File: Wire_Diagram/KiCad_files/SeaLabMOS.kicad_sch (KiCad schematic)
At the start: 17 parts

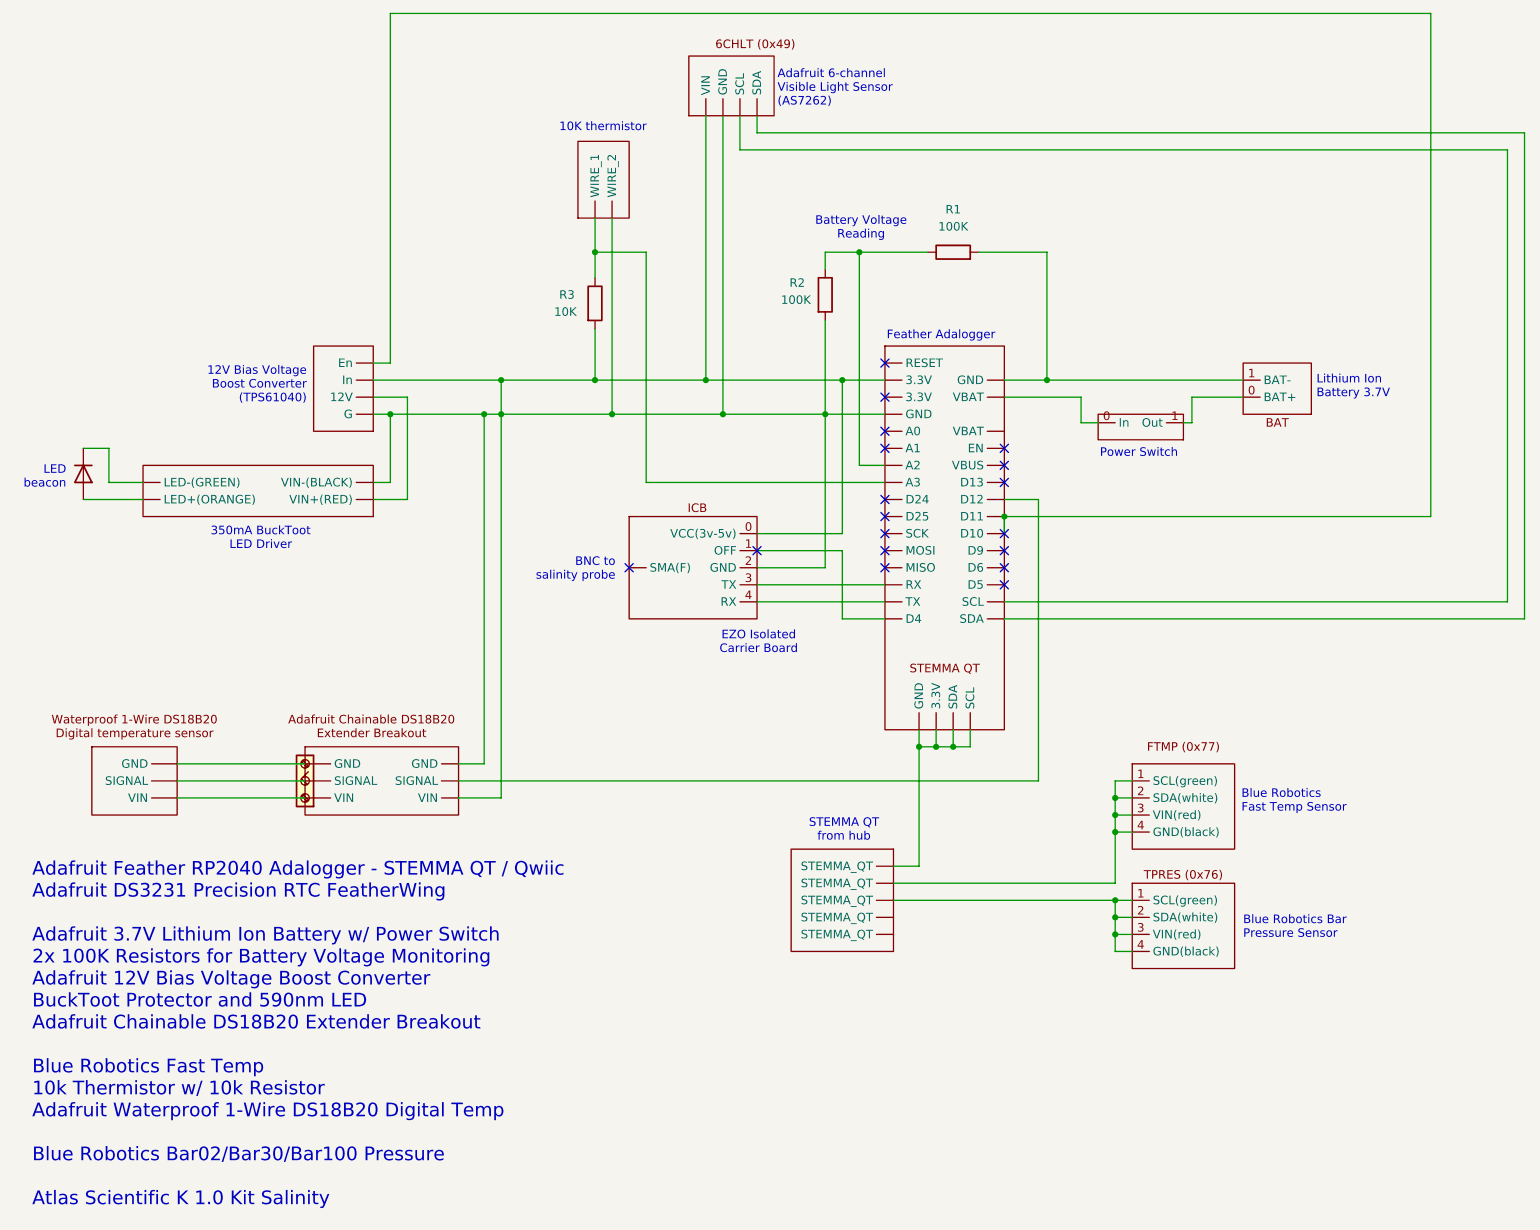
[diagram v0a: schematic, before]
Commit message: added GNSS
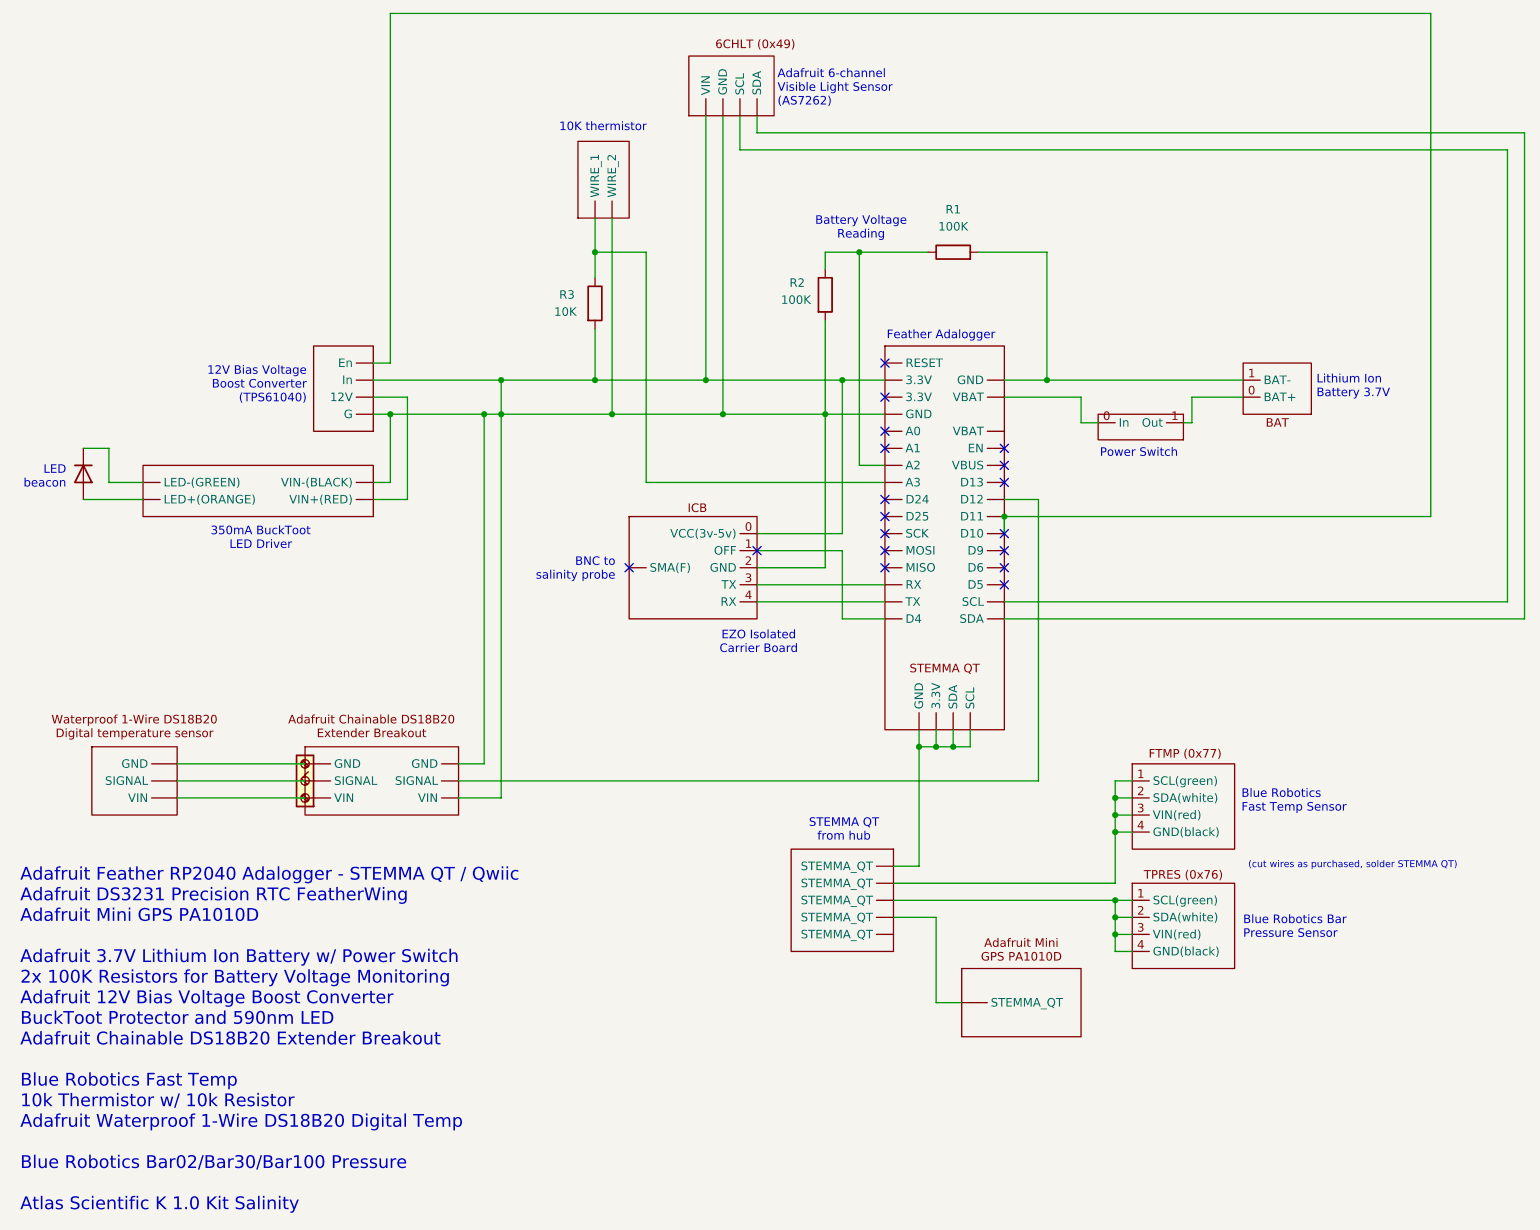
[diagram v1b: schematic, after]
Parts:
- added U14: ~, symbol ctd:Adafruit_Mini_GPS_PA1010D
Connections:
- net at U13. (VIN): now also U8. (VBUS); no longer U12. (VIN)
- net at U11. (STEMMA_QT): now also U2.1 (SCL(green)), U2.2 (SDA(white)), U2.3 (VIN(red)), U2.4 (GND(black))
- net at U8. (VBUS): now also U10. (VIN); no longer U11. (STEMMA_QT)
- new net: U11. (STEMMA_QT), U14. (STEMMA_QT)
- new net: U12. (VIN), U13. (VIN) (x2)
- new net: R2.2, R3.2, U10. (VIN), U13. (VIN), U3. (VIN-(BLACK)), U4. (In), U6.0 (VCC(3v-5v)), U6.2 (GND), U8. (VBUS), U9. (WIRE_2)
- new net: U11. (STEMMA_QT), U8. (VBUS)
- new net: U10. (VIN), U8. (VBUS)
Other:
- note added: "(cut wires as purchased, solder STEMMA QT)"
- note added: "Adafruit Feather RP2040 Adalogger - STEMMA QT / Qwiic Adafruit DS3231 Precision RTC FeatherWing Adafruit Mini GPS PA1010D Adafruit 3.7V Lithium Ion Battery w/ Power Switch 2x 100K Resistors for Battery Voltage Monitoring Adafruit 12V Bias Voltage Boost Converter BuckToot Protector and 590nm LED Adafruit Chainable DS18B20 Extender Breakout Blue Robotics Fast Temp 10k Thermistor w/ 10k Resistor Ada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"
- note removed: "Adafruit Feather RP2040 Adalogger - STEMMA QT / Qwiic Adafruit DS3231 Precision RTC FeatherWing Adafruit 3.7V Lithium Ion Battery w/ Power Switch 2x 100K Resistors for Battery Voltage Monitoring Adafruit 12V Bias Voltage Boost Converter BuckToot Protector and 590nm LED Adafruit Chainable DS18B20 Extender Breakout Blue Robotics Fast Temp 10k Thermistor w/ 10k Resistor Adafruit Waterproof 1-Wire DS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"
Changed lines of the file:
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@@
 		(company "Aspect Wave LLC")
 		(comment 1 "LED beacon on heatsink")
-		(comment 2 "All sensors listed bottom left")
+		(comment 2 "STEMMA QT ports simplified")
+		(comment 3 "All sensors listed bottom left")
 	)
 	(junction
@@
 	(wire
 		(pts
+			(xy 149.86 152.4) (xy 149.86 165.1)
+		)
+		(stroke
+			(width 0)
+			(type default)
+		)
+	)
+	(wire
+		(pts
 			(xy 237.49 35.56) (xy 237.49 107.95)
 		)
@@
 	(wire
 		(pts
+			(xy 143.51 152.4) (xy 149.86 152.4)
+		)
+		(stroke
+			(width 0)
+			(type default)
+		)
+	)
+	(wire
+		(pts
 			(xy 187.96 74.93) (xy 195.58 74.93)
 		)
@@
 	(wire
 		(pts
+			(xy 149.86 165.1) (xy 153.67 165.1)
+		)
+		(stroke
+			(width 0)
+			(type default)
+		)
+	)
+	(wire
+		(pts
 			(xy 166.37 72.39) (xy 195.58 72.39)
 		)
@@
 			(width 0)
 			(type default)
+		)
+	)
+	(text "(cut wires as purchased, solder STEMMA QT)"
+		(exclude_from_sim no)
+		(at 196.342 145.288 0)
+		(effects
+			(font
+				(size 1.016 1.016)
+			)
+			(justify left bottom)
 		)
 	)
@@
 		)
 	)
-	(text "Adafruit Feather RP2040 Adalogger - STEMMA QT / Qwiic\nAdafruit DS3231 Precision RTC FeatherWing\n\nAdafruit 3.7V Lithium Ion Battery w/ Power Switch\n2x 100K Resistors for Battery Voltage Monitoring\nAdafruit 12V Bias Voltage Boost Converter\nBuckToot Protector and 590nm LED\nAdafruit Chainable DS18B20 Extender Breakout\n\nBlue Robotics Fast Temp\n10k Thermistor w/ 10k Resistor\nAdafruit Waterproof 1-Wire DS18B20 Digital Temp\n\nBlue Robotics Bar02/Bar30/Bar100 Pressure\n\nAtlas Scientific K 1.0 Kit Salinity\n\n"
-		(exclude_from_sim no)
-		(at 15.24 198.882 0)
+	(text "Adafruit Feather RP2040 Adalogger - STEMMA QT / Qwiic\nAdafruit DS3231 Precision RTC FeatherWing\nAdafruit Mini GPS PA1010D\n\nAdafruit 3.7V Lithium Ion Battery w/ Power Switch\n2x 100K Resistors for Battery Voltage Monitoring\nAdafruit 12V Bias Voltage Boost Converter\nBuckToot Protector and 590nm LED\nAdafruit Chainable DS18B20 Extender Breakout\n\nBlue Robotics Fast Temp\n10k Thermistor w/ 10k Resistor\nAdafruit Waterproof 1-Wire DS18B20 Digital Temp\n\nBlue Robotics Bar02/Bar30/Bar100 Pressure\n\nAtlas Scientific K 1.0 Kit Salinity"
+		(exclude_from_sim no)
+		(at 13.462 196.342 0)
 		(effects
 			(font
-				(size 2.032 2.032)
+				(size 1.905 1.905)
+				(thickness 0.2381)
 			)
 			(justify left bottom)
@@
 					(unit 1)
 				)
+			)
+		)
+	)
+	(symbol
+		(lib_id "ctd:Adafruit_Mini_GPS_PA1010D")
+		(at 157.48 158.75 0)
+		(unit 1)
+		(exclude_from_sim no)
+		(in_bom yes)
+		(on_board yes)
+		(dnp no)
+		(fields_autoplaced yes)
+		(property "Reference" "U14"
+			(at 157.48 158.75 0)
+			(effects
+				(font
+					(size 1.27 1.27)
+				)
+				(hide yes)
+			)
+		)
+		(property "Value" "~"
+			(at 172.72 162.681 0)
+			(effects
+				(font
+					(size 1.27 1.27)
+				)
+				(justify left)
+			)
+		)
+		(property "Footprint" ""
+			(at 157.48 158.75 0)
+			(effects
+				(font
+					(size 1.27 1.27)
+				)
+				(hide yes)
+			)
+		)
+		(property "Datasheet" ""
+			(at 157.48 158.75 0)
+			(effects
+				(font
+					(size 1.27 1.27)
+				)
+				(hide yes)
+			)
+		)
+		(property "Description" ""
+			(at 157.48 158.75 0)
+			(effects
+				(font
+					(size 1.27 1.27)
+				)
+				(hide yes)
+			)
+		)
+		(pin ""
+		)
+		(instances
+			(project ""
+				(path "/2b88df0d-ed83-4383-9471-7e748ad5f29a"
+					(reference "U14")
+					(unit 1)
+				)
